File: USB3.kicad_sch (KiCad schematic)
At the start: 13 parts, among them J1901 USB_C_Receptacle, J1902 USB_C_Receptacle, U1901 AP22653W6-7

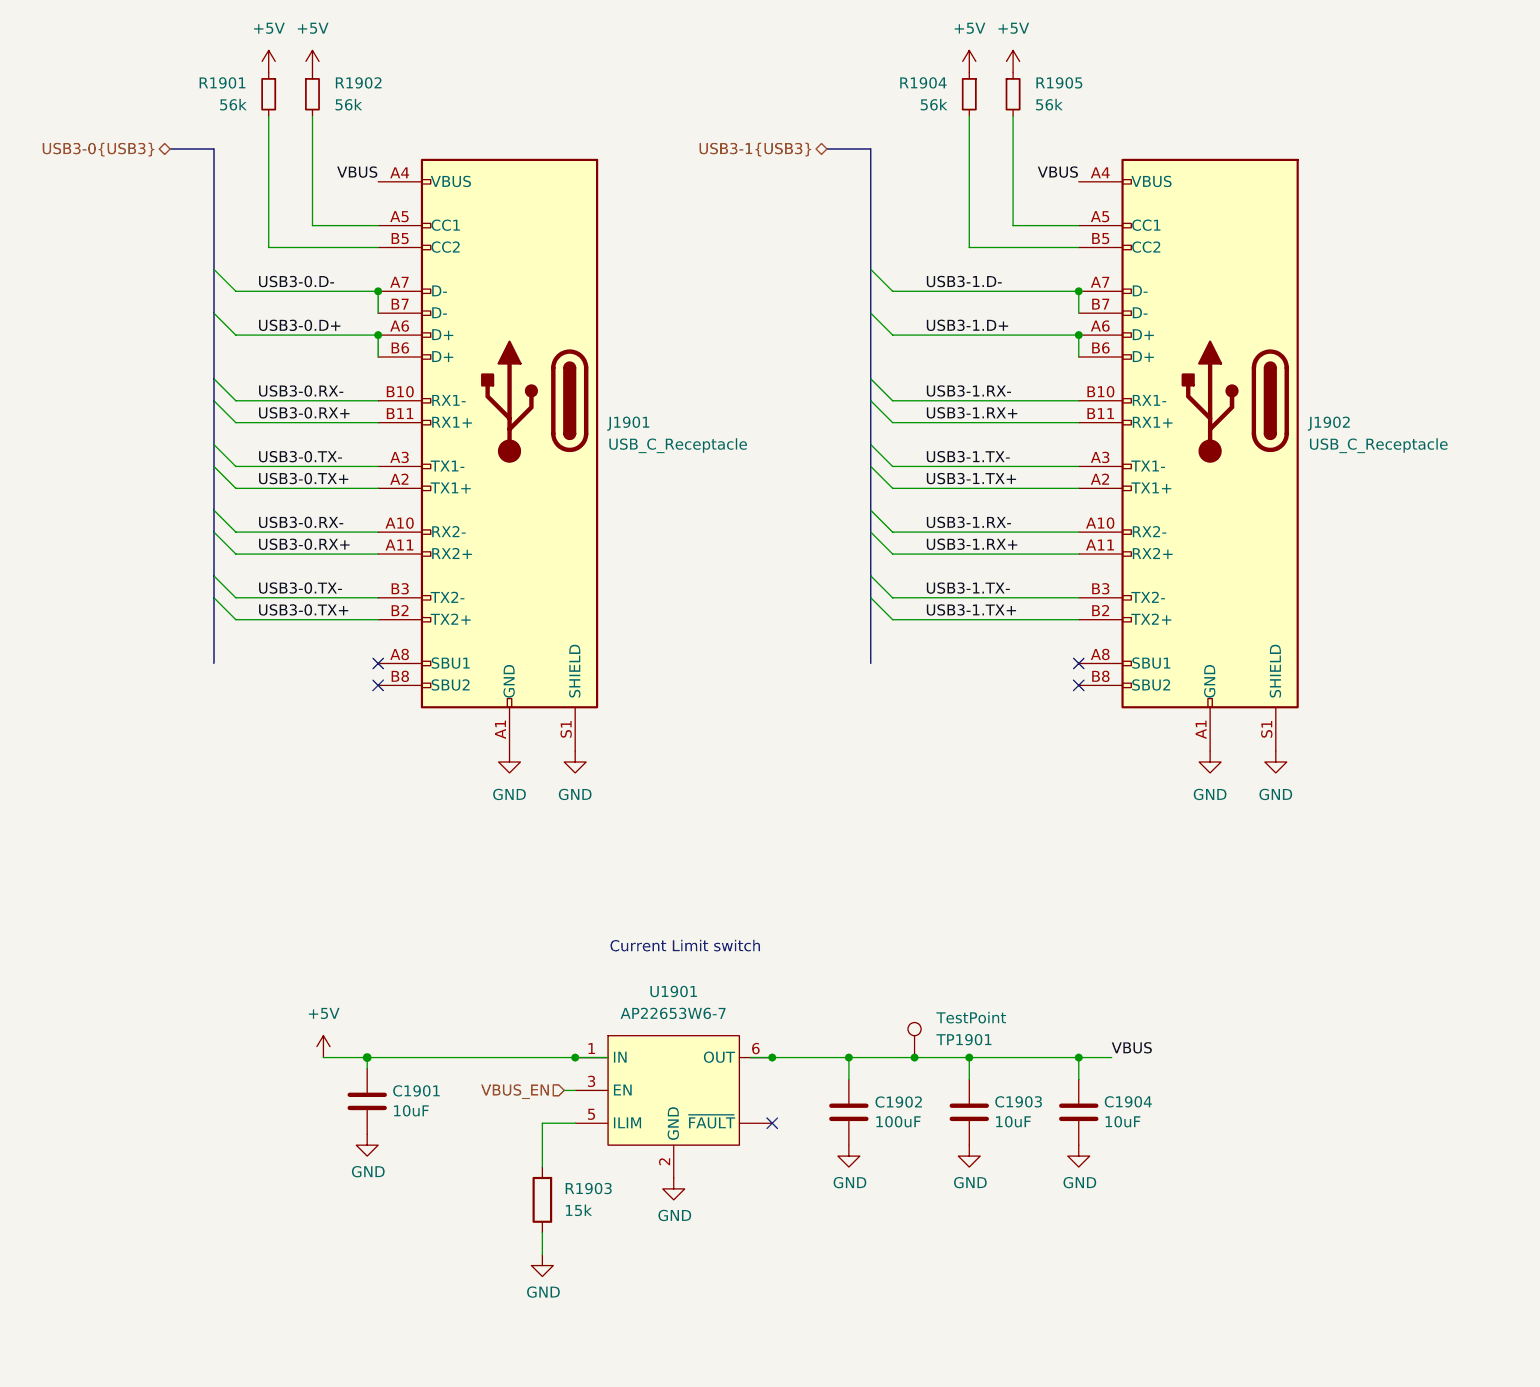
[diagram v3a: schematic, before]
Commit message: Revert USB3 ports back to Type A
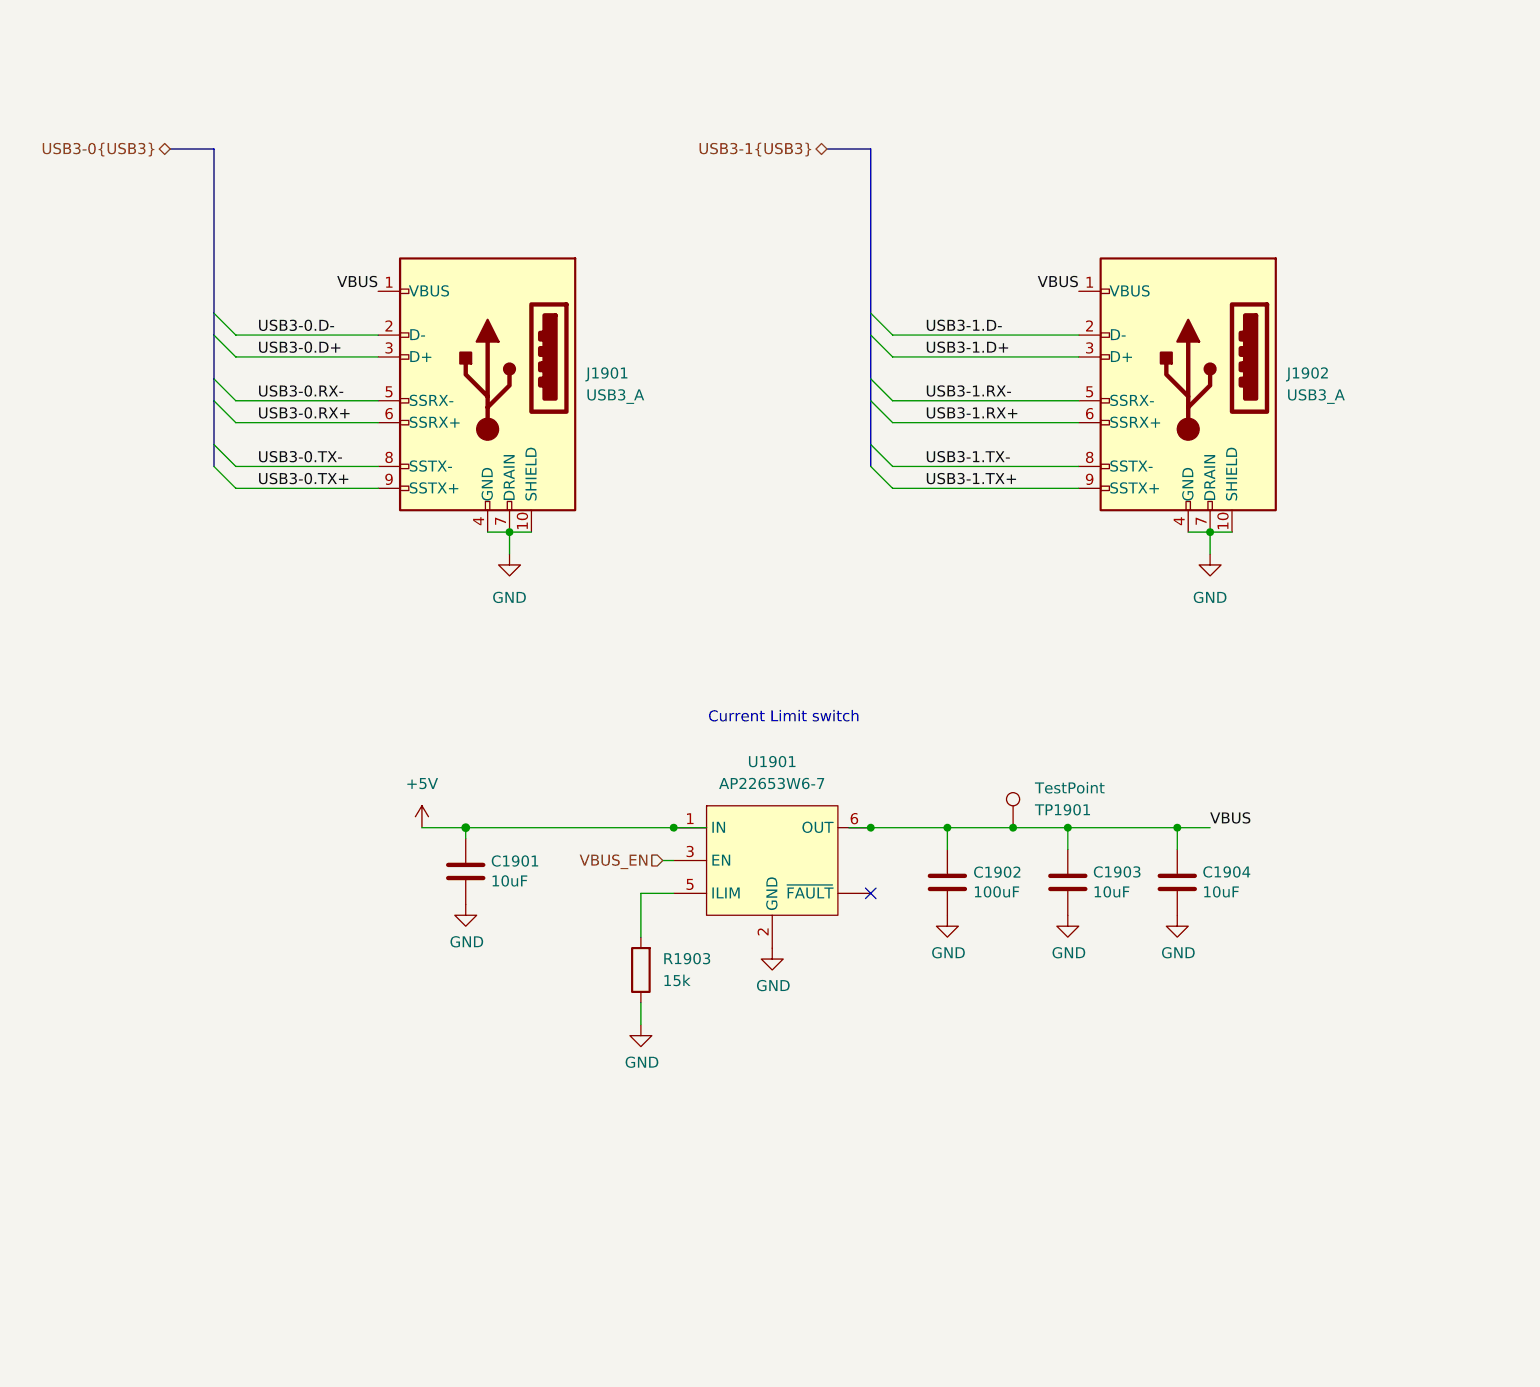
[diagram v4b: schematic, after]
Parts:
- removed J1901, J1902: USB_C_Receptacle, Hatlabs:USB_TYPE-C_SHOU-HAN_24PLT-H10.5-1, symbol Connector:USB_C_Receptacle
- removed R1901, R1902, R1904, R1905: 56k, Resistor_SMD:R_0402_1005Metric, symbol Device:R_Small
- added J1901, J1902: USB3_A, Hatlabs:USB-3.0-TH_USB-302LD-ARW, symbol Connector:USB3_A
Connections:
- net GND: now also J1901.10 (SHIELD), J1901.4 (GND), J1901.7 (DRAIN), J1902.10 (SHIELD), J1902.4 (GND), J1902.7 (DRAIN)
- net USB3-0.D+: now also J1901.3 (D+)
- net USB3-0.D-: now also J1901.2 (D-)
- net USB3-0.RX+: now also J1901.6 (SSRX+)
- net USB3-0.RX-: now also J1901.5 (SSRX-)
- net USB3-0.TX+: now also J1901.9 (SSTX+)
- net USB3-0.TX-: now also J1901.8 (SSTX-)
- net USB3-1.D+: now also J1902.3 (D+)
- net USB3-1.D-: now also J1902.2 (D-)
- net USB3-1.RX+: now also J1902.6 (SSRX+)
- net USB3-1.RX-: now also J1902.5 (SSRX-)
- net USB3-1.TX+: now also J1902.9 (SSTX+)
- net USB3-1.TX-: now also J1902.8 (SSTX-)
- net VBUS: now also J1901.1 (VBUS), J1902.1 (VBUS)
- no-connect marks 5 -> 1
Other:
- moved on the sheet: C1901, C1902, C1903, C1904, R1903, TP1901, U1901

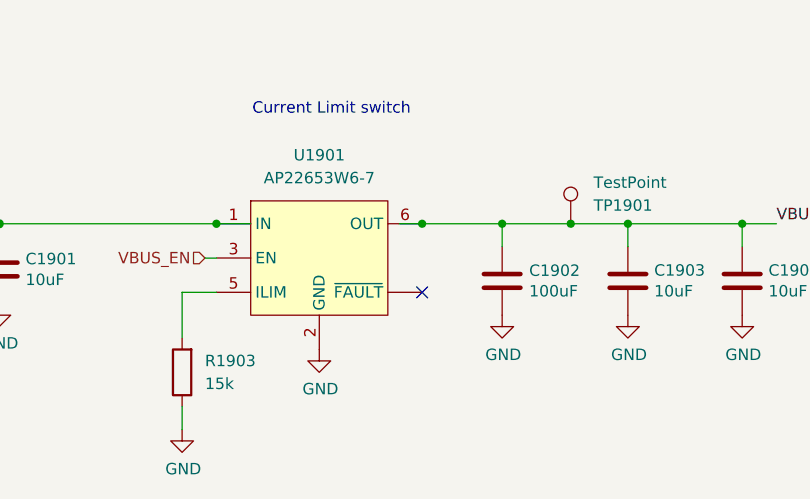
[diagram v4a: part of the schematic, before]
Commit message: Fix ethernet port & other changes
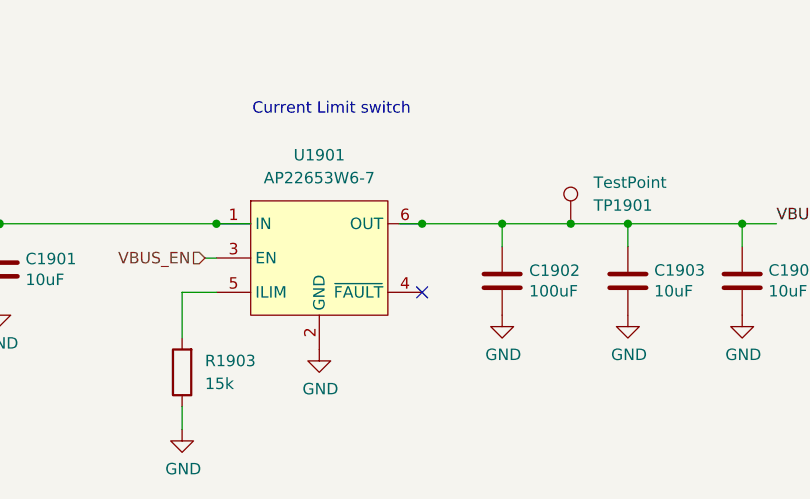
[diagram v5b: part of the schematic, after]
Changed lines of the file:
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@@
 			)
 		)
-		(pin ""
+		(pin "4"
 		)
 		(pin "3"

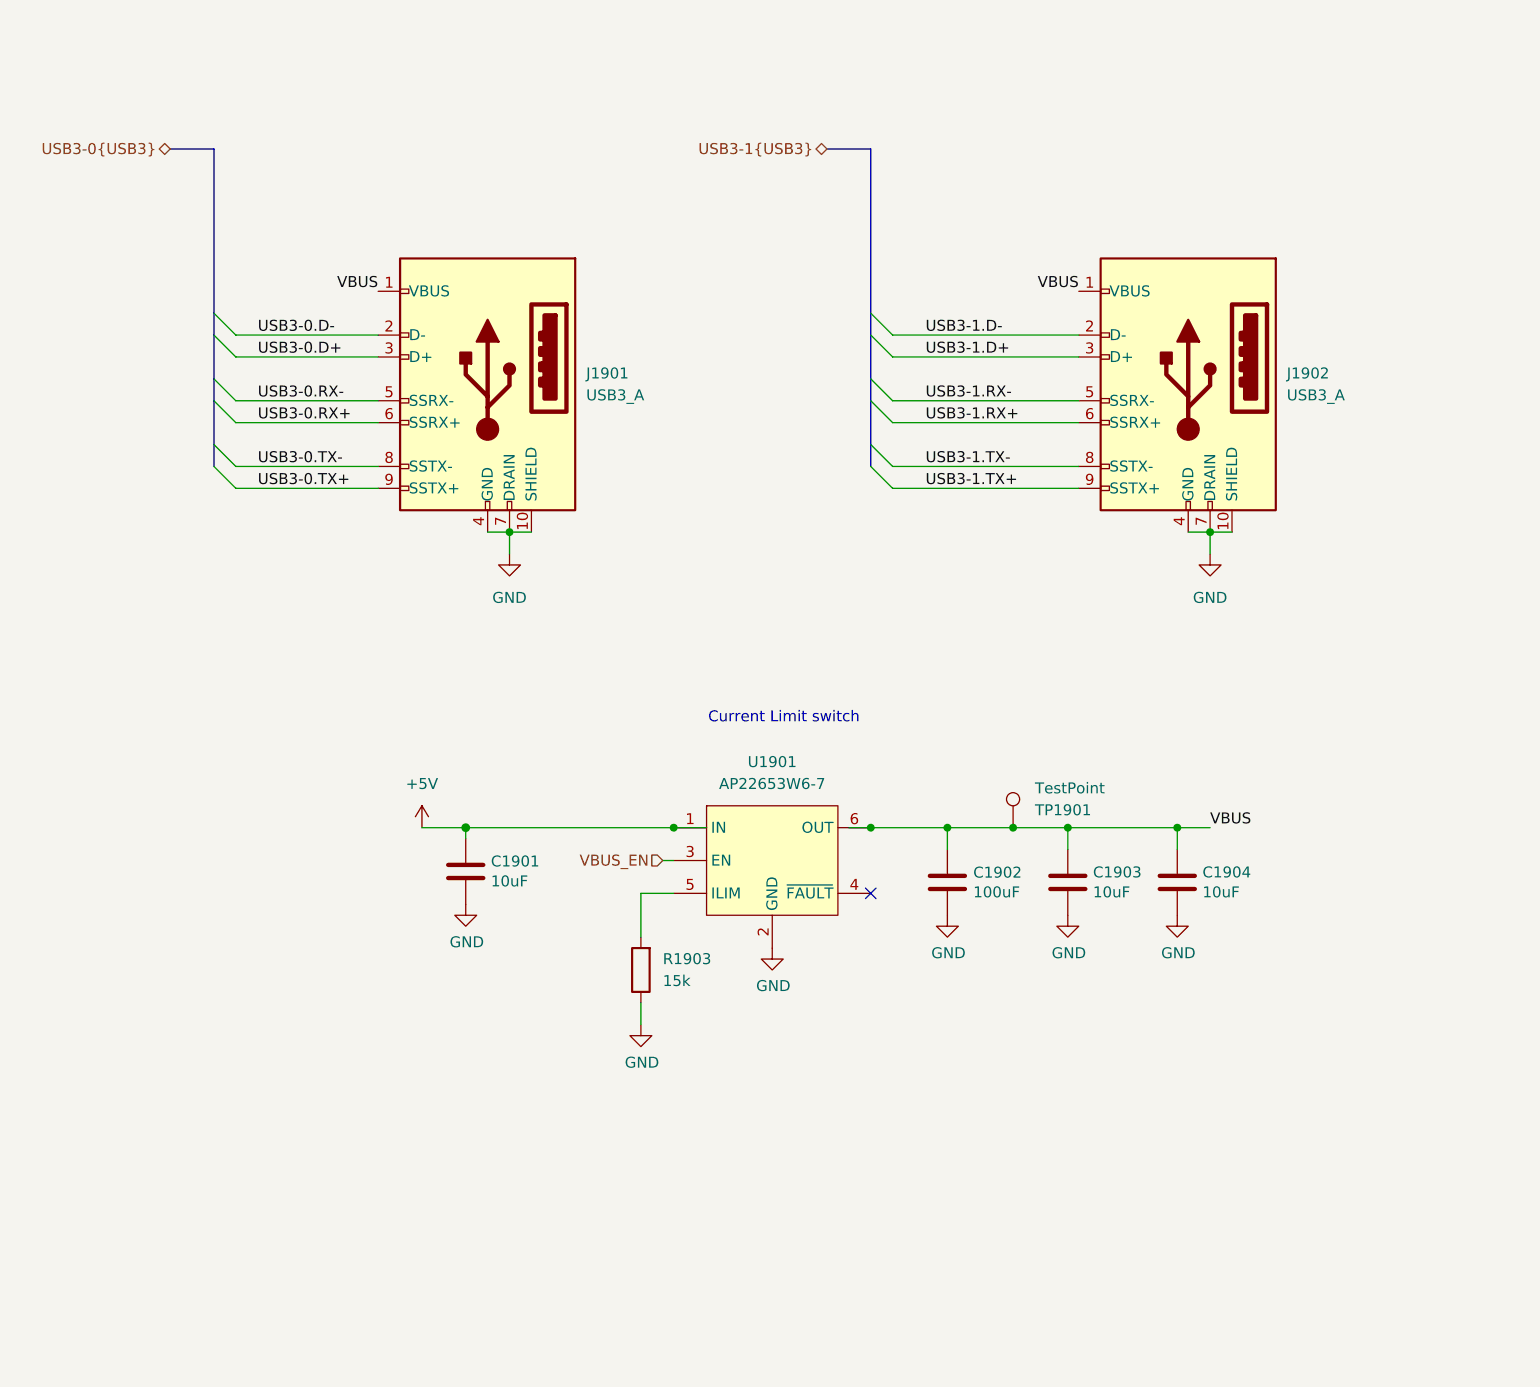
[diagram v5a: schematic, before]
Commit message: Implement a USB3 hub
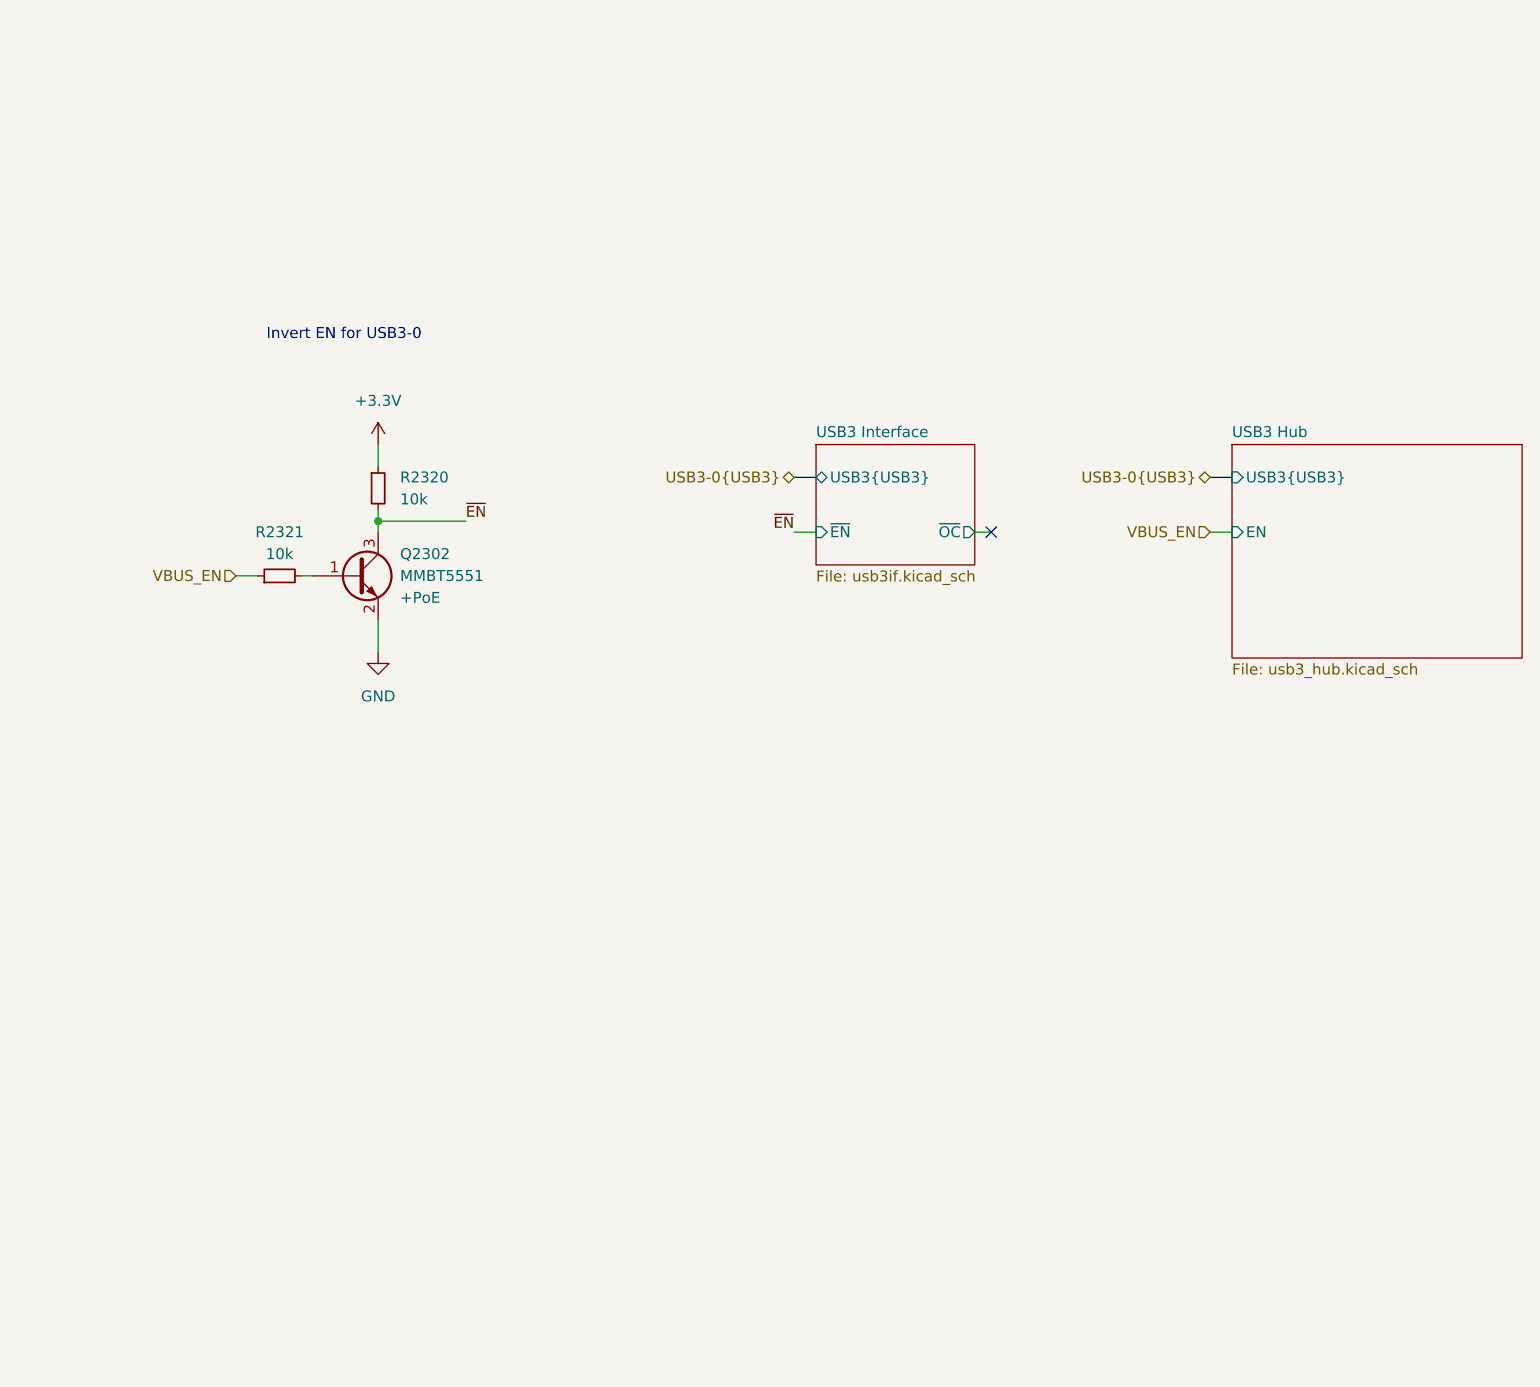
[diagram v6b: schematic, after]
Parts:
- removed C1901, C1903, C1904: 10uF, Capacitor_SMD:C_0805_2012Metric, symbol Device:C
- removed C1902: 100uF, Capacitor_SMD:C_1210_3225Metric, symbol Device:C
- removed J1901, J1902: USB3_A, Hatlabs:USB-3.0-TH_USB-302LD-ARW, symbol Connector:USB3_A
- removed R1903: 15k, Resistor_SMD:R_0402_1005Metric, symbol Device:R
- removed TP1901: TestPoint, TestPoint:TestPoint_Pad_D1.0mm, symbol Connector:TestPoint
- removed U1901: AP22653W6-7, Package_TO_SOT_SMD:SOT-23-6, symbol Hatlabs:AP22653
- added Q2302: MMBT5551, Package_TO_SOT_SMD:SOT-23, symbol Transistor_BJT:MMBTA42
- added R2320, R2321: 10k, symbol Device:R_Small
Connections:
- net GND: now also Q2302.2 (E)
- net VBUS_EN: now also R2321.1
- new net: Q2302.1 (B), R2321.2
- new net +3.3V: R2320.1
- new net ~{EN}: Q2302.3 (C), R2320.2
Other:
- added sheet USB3 Hub (usb3_hub.kicad_sch)
- added sheet USB3 Interface (usb3if.kicad_sch)
- note added: "Invert EN for USB3-0"
- note removed: "Current Limit switch"

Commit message: Finish component selection for USB3 hub
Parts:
- R2320, R2321: footprint (none) -> Resistor_SMD:R_0402_1005Metric; LCSC (none) -> C25744
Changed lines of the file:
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@@
 			)
 		)
-		(property "Footprint" ""
+		(property "Footprint" "Resistor_SMD:R_0402_1005Metric"
 			(at 80.01 88.9 0)
 			(effects
@@
 		)
 		(property "Description" "Resistor, small symbol"
+			(at 80.01 88.9 0)
+			(effects
+				(font
+					(size 1.27 1.27)
+				)
+				(hide yes)
+			)
+		)
+		(property "LCSC" "C25744"
 			(at 80.01 88.9 0)
 			(effects
@@
 			)
 		)
-		(property "Footprint" ""
+		(property "Footprint" "Resistor_SMD:R_0402_1005Metric"
 			(at 68.58 99.06 0)
 			(effects
@@
 			(at 68.58 99.06 0)
 			(effects
+				(font
+					(size 1.27 1.27)
+				)
+				(hide yes)
+			)
+		)
+		(property "LCSC" "C25744"
+			(at 68.58 99.06 0)
+			(effects
